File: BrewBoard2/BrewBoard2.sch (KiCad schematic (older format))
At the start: 29 parts, among them J2 Conn_01x02, J3 Conn_01x03, J4 Conn_01x03, J5 Conn_01x03, J81 J8Header, J82 J8Header, Q1 BC337, Q2 BC337

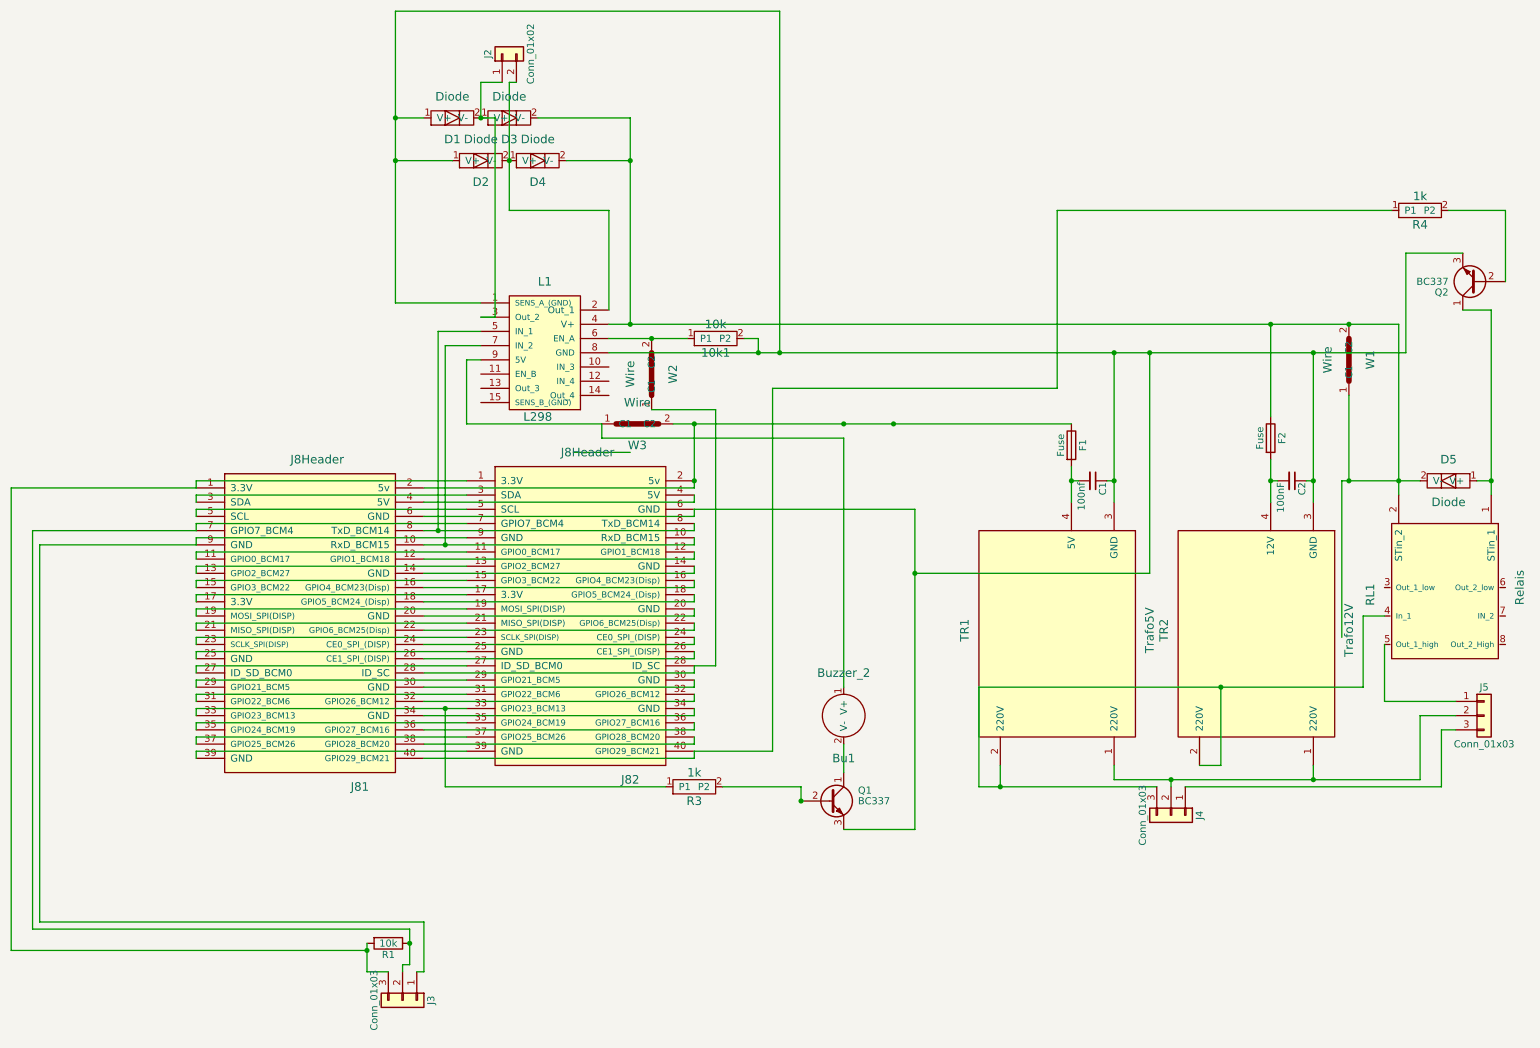
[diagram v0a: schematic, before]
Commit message: second design with turned header
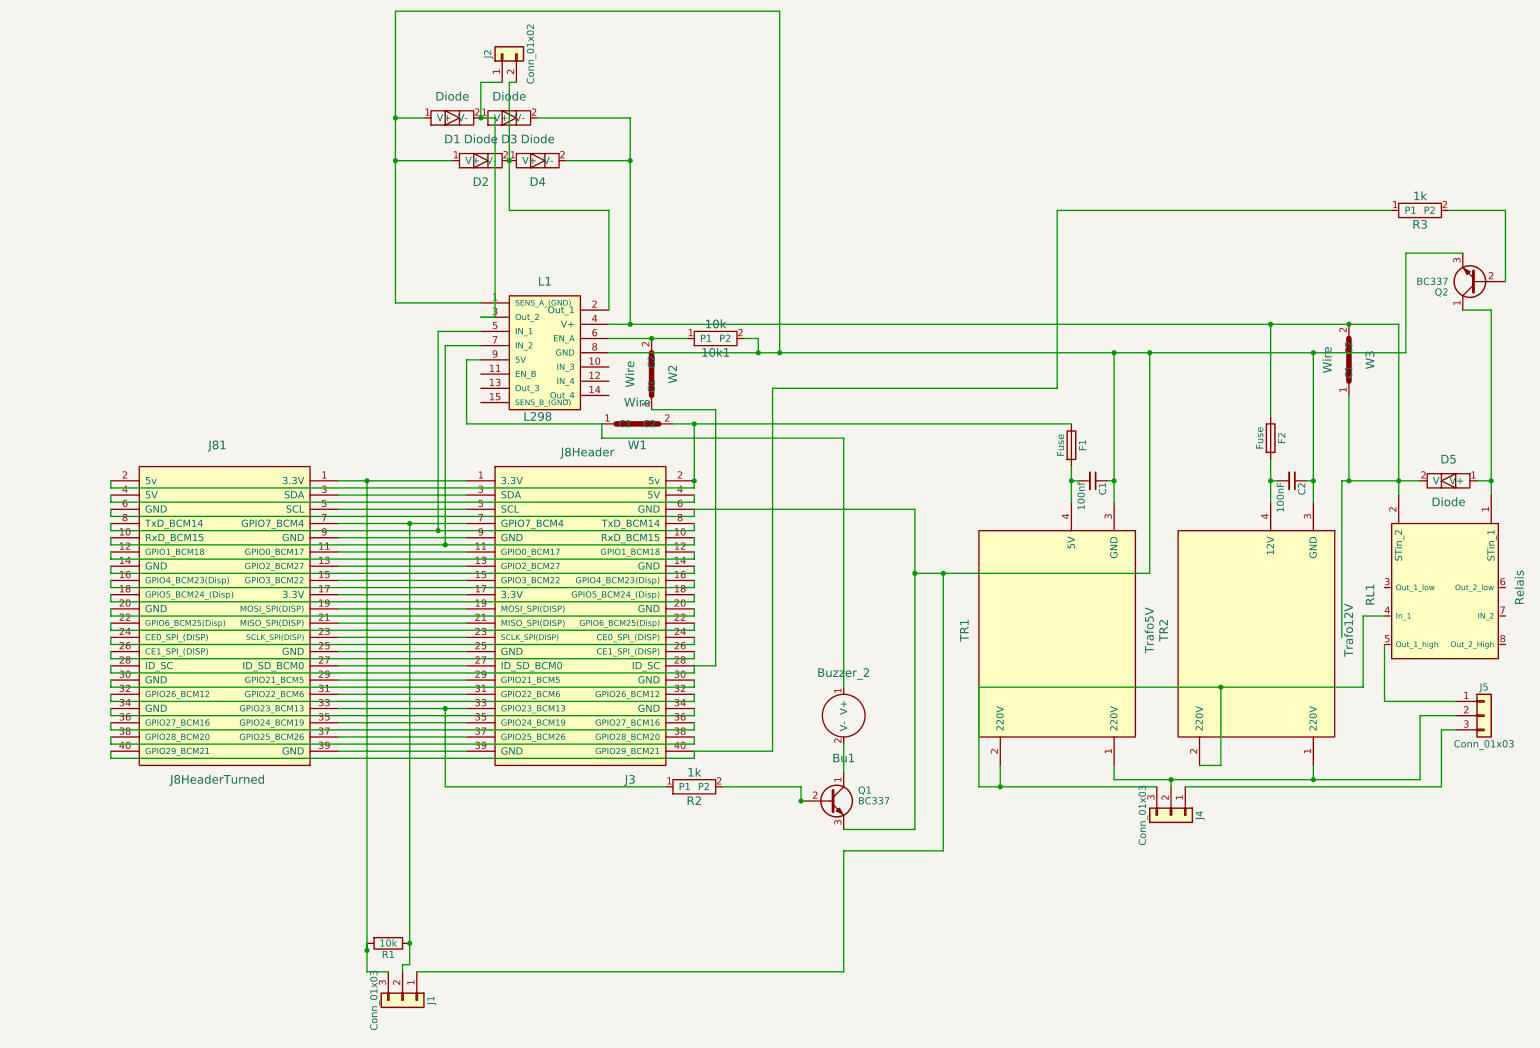
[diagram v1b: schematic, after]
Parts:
- removed J3: Conn_01x03, RasperryLib:Conn_Small1x3, symbol Conn_01x03
- removed J81, J82: J8Header, RasperryLib:RaspiConnector, symbol J8Header
- removed R4: 1k, RasperryLib:Resistor, symbol Resistor
- added J1: Conn_01x03, RasperryLib:Conn_Small1x3, symbol Conn_01x03
- added J3: J8Header, RasperryLib:RaspiConnector, symbol J8Header
- added J81: J8HeaderTurned, RasperryLib:RaspiConnectorTurned, symbol J8HeaderTurned
- added R2: 1k, RasperryLib:Resistor, symbol Resistor
- W1: footprint RasperryLib:Wire_Short -> RasperryLib:Wire_long
- W3: footprint RasperryLib:Wire_long -> RasperryLib:Wire_Short
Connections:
- net at R1.1: now also J1.2 (Pin_2), J3.7 (GPIO7_BCM4), J81.7 (GPIO7_BCM4)
- net at R1.2: now also J1.3 (Pin_3), J3.1 (3.3V), J81.1 (3.3V)
- net at 10k1.2 (P2), C1.1, C2.1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: now also J1.1 (Pin_1), J3.6 (GND), J81.6 (GND)
- net at D3.2 (V-), D4.2 (V-), D5.2 (V-)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: now also W3.1 (C1), W3.2 (C2); no longer W1.1 (C1), W1.2 (C2)
- net at L1.5 (IN_1): now also J3.8 (TxD_BCM14), J81.8 (TxD_BCM14)
- net at L1.7 (IN_2): now also J3.10 (RxD_BCM15), J81.10 (RxD_BCM15)
- net at Bu1.1 (V+), L1.9 (5V): now also W1.1 (C1); no longer W3.1 (C1)
- net at F1.1: now also W1.2 (C2), J3.2 (5v), J81.2 (5v); no longer W3.2 (C2)
- net at Q1.2 (B): now also R2.2 (P2); no longer R3.2 (P2)
- net at R3.1 (P1): now also J3.40 (GPIO29_BCM21), J81.40 (GPIO29_BCM21)
- net at Q2.2 (B): now also R3.2 (P2)
- net at W2.1 (C1): now also J3.28 (ID_SC), J81.28 (ID_SC)
- new net: J3.33 (GPIO23_BCM13), J81.33 (GPIO23_BCM13), R2.1 (P1)
- new net: J3.11 (GPIO0_BCM17), J81.11 (GPIO0_BCM17)
- new net: J3.12 (GPIO1_BCM18), J81.12 (GPIO1_BCM18)
- new net: J3.13 (GPIO2_BCM27), J81.13 (GPIO2_BCM27)
- new net: J3.14 (GND), J81.14 (GND)
- new net: J3.15 (GPIO3_BCM22), J81.15 (GPIO3_BCM22)
- new net: J3.16 (GPIO4_BCM23(Disp)), J81.16 (GPIO4_BCM23(Disp))
- new net: J3.17 (3.3V), J81.17 (3.3V)
- new net: J3.18 (GPIO5_BCM24_(Disp)), J81.18 (GPIO5_BCM24_(Disp))
- new net: J3.19 (MOSI_SPI(DISP)), J81.19 (MOSI_SPI(DISP))
- new net: J3.20 (GND), J81.20 (GND)
- new net: J3.21 (MISO_SPI(DISP)), J81.21 (MISO_SPI(DISP))
- new net: J3.22 (GPIO6_BCM25(Disp)), J81.22 (GPIO6_BCM25(Disp))
- new net: J3.23 (SCLK_SPI(DISP)), J81.23 (SCLK_SPI(DISP))
- new net: J3.24 (CE0_SPI_(DISP)), J81.24 (CE0_SPI_(DISP))
- new net: J3.25 (GND), J81.25 (GND)
- new net: J3.26 (CE1_SPI_(DISP)), J81.26 (CE1_SPI_(DISP))
- new net: J3.27 (ID_SD_BCM0), J81.27 (ID_SD_BCM0)
- new net: J3.29 (GPIO21_BCM5), J81.29 (GPIO21_BCM5)
- new net: J3.3 (SDA), J81.3 (SDA)
- new net: J3.30 (GND), J81.30 (GND)
- new net: J3.31 (GPIO22_BCM6), J81.31 (GPIO22_BCM6)
- new net: J3.32 (GPIO26_BCM12), J81.32 (GPIO26_BCM12)
- new net: J3.34 (GND), J81.34 (GND)
- new net: J3.35 (GPIO24_BCM19), J81.35 (GPIO24_BCM19)
- new net: J3.36 (GPIO27_BCM16), J81.36 (GPIO27_BCM16)
- new net: J3.37 (GPIO25_BCM26), J81.37 (GPIO25_BCM26)
- new net: J3.38 (GPIO28_BCM20), J81.38 (GPIO28_BCM20)
- new net: J3.39 (GND), J81.39 (GND)
- new net: J3.4 (5V), J81.4 (5V)
- new net: J3.5 (SCL), J81.5 (SCL)
- new net: J3.9 (GND), J81.9 (GND)
